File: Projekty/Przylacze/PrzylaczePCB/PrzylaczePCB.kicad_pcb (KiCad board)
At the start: 2 copper layers, 134.6 x 126 mm, 131 parts, among them J1 Conn_02x20_Odd_Even, J2 USB_B, J3 Conn_01x06, J4 Conn_02x04_Odd_Even, J5 Screw_Terminal_01x06, M3 MountingHole_3.2mm_M3, Q1 BC547, Q10 BC557, Q11 2N3904, Q12 2N7002, Q2 BC547, Q3 BC547, Q4 BC557, Q5 2N3904, Q6 BC557, Q7 BC557, Q8 BC547, Q9 BC557, SW1 SW_Push, SW2 SW_SPDT, SW3 SW_SPDT, SW4 SW_SPDT, SW5 SW_SPDT, SW6 SW_SPDT, SW7 SW_SPDT, SW8 SW_SPDT, SW9 SW_SPDT, U1 MCP2561-E-P, U2 ATSAM4S2AA-AU, U3 MCP2515-xSO, U4 TJA1055T_3_C,518, U5 MAX3485, U6 74AHC1G04, U7 LDL1117S33R, U8 DI78M05UAB, U9 74AHC1G04, Y1 20MHz

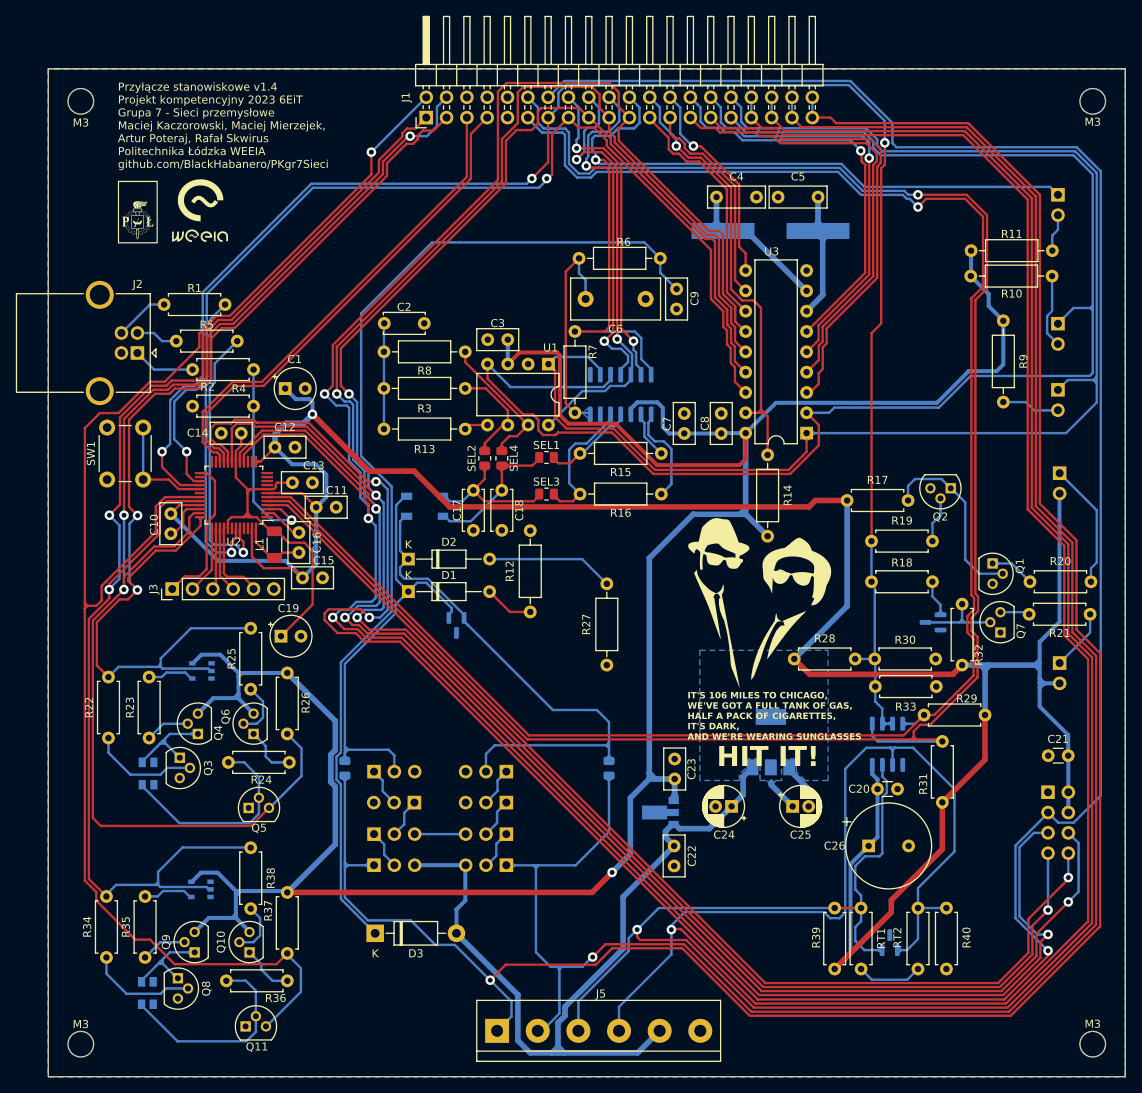
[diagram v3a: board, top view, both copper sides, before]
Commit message: Przyłącze - projekt PCB v1.5
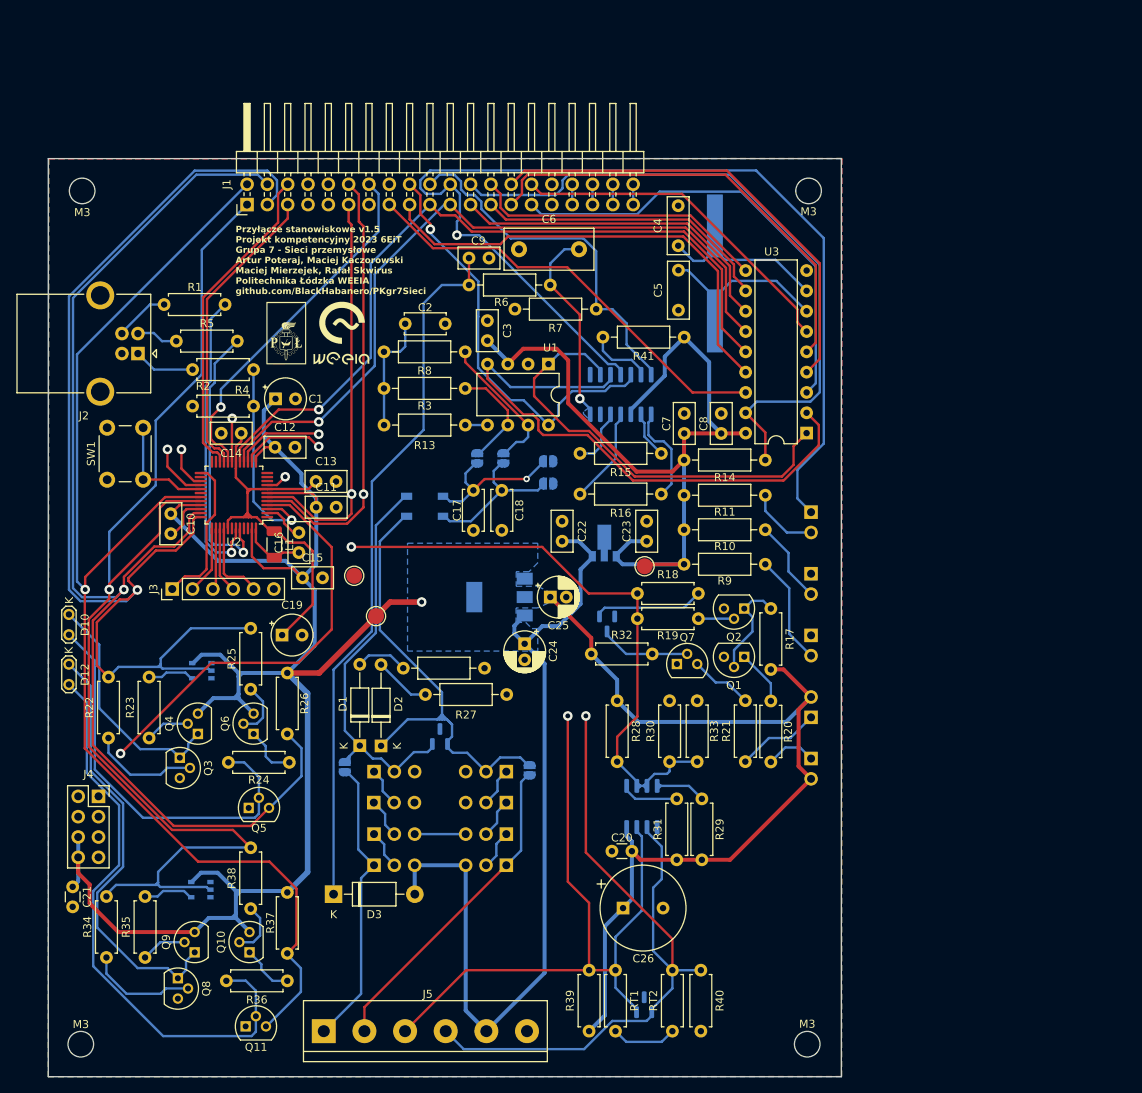
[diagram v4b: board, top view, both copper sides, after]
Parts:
- removed the G*** at (129.1, 137.9)
- added R41: 10k, Resistor_THT:R_Axial_DIN0207_L6.3mm_D2.5mm_P10.16mm_Horizontal, F.Cu at (119.6, 104.7)
- added REF**: TestPoint_Pad_D2.0mm, TestPoint:TestPoint_Pad_D2.0mm, F.Cu at (114.7, 133.3)
- added REF**: TestPoint_Pad_D2.0mm, TestPoint:TestPoint_Pad_D2.0mm, F.Cu at (81.1, 139.5)
- added REF**: TestPoint_Pad_D2.0mm, TestPoint:TestPoint_Pad_D2.0mm, F.Cu at (78.4, 134.5)
- D10, D12: footprint LED_SMD:LED_Kingbright_AAA3528ESGCT -> TestPoint:TestPoint_2Pads_Pitch2.54mm_Drill0.8mm; moved to F.Cu
- J4: moved to F.Cu
- R7: value >1k8 -> 1k
- SEL1, SEL2, SEL3, SEL4: footprint Resistor_SMD:R_0805_2012Metric -> Jumper:SolderJumper-2_P1.3mm_Open_RoundedPad1.0x1.5mm; moved to B.Cu
- SEL5, SEL6: footprint Resistor_SMD:R_0805_2012Metric -> Jumper:SolderJumper-2_P1.3mm_Open_RoundedPad1.0x1.5mm
- moved C21 123.4 mm to (43.2, 175.9), turned to 90 degrees
- moved J4 118.7 mm to (46.4, 162.1), turned to 0 degrees
- moved D4 50.3 mm to (135.5, 126.5)
- moved R10 47.9 mm to (129.8, 128.7)
- moved D7 47.3 mm to (135.5, 157.3)
- moved R11 47.1 mm to (129.8, 124.4)
- moved R21 46.9 mm to (127.3, 157.7), turned to 90 degrees
- moved R32 46.4 mm to (108.0, 144.3), turned to 0 degrees
- moved R20 45.9 mm to (130.4, 157.8), turned to 90 degrees
- moved C22 45.3 mm to (104.4, 127.7), turned to -90 degrees
- moved D6 43.9 mm to (135.5, 134.2)
- moved D5 43.5 mm to (135.5, 141.9)
- moved D12 42.3 mm to (42.7, 145.5)
- moved Q12 40.7 mm to (110.0, 140.5), turned to -90 degrees
- moved Q7 40.6 mm to (118.7, 145.5), turned to 0 degrees
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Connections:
- D9 pad 1: Net-(D1-K) -> Net-(D2-K)
- D9 pad 2: Net-(D2-K) -> Net-(D1-K)
- J1 pad 18: STB_FT -> STBY
- J1 pad 27: TX0RTS -> TX1RTS
- J1 pad 28: TX2RTS -> TX0RTS
- J1 pad 30: TX1RTS -> TX2RTS
- J1 pad 33: A -> B
- J1 pad 34: A -> B
- J1 pad 35: B -> A
- J1 pad 36: B -> A
- J1 pad 37: CANL -> CANH
- J1 pad 38: CANL -> CANH
- J1 pad 39: CANH -> CANL
- J1 pad 40: CANH -> CANL
- J1 pad 5: UART0_RX -> UART0_TX
- J1 pad 6: GND -> UART0_RX
- J1 pad 7: UART0_TX -> GND
- J4 pad 1: GND -> MISO
- J4 pad 2: +3.3V -> RADIO_IRQ
- J4 pad 3: CS0 -> SPCK
- J4 pad 4: +3.3V -> MOSI
- J4 pad 5: SPCK -> CS0
- J4 pad 6: MOSI -> +3.3V
- J4 pad 7: MISO -> GND
- J4 pad 8: RADIO_IRQ -> +3.3V
- Q10 pad 3: +5V -> +3.3V
- Q4 pad 3: +5V -> +3.3V
- Q6 pad 3: +5V -> +3.3V
- Q9 pad 3: +5V -> +3.3V
- R15 pad 2: CANH_FT -> CANL_FT
- R16 pad 1: Net-(U4-RTH) -> CANH_FT
- R16 pad 2: CANL_FT -> Net-(U4-RTH)
- R26 pad 2: +5V -> +3.3V
- R37 pad 2: +5V -> +3.3V
- R7 pad 2: Net-(U4-BAT) -> GND
- U1 pad 8: STB_FT -> STBY
- U2 pad 14: unconnected-(U2-PA16/PGMD4-Pad14) -> STBY
- U2 pad 15: unconnected-(U2-PA15/PGMD3-Pad15) -> EN
- U2 pad 9: unconnected-(U2-PA17/PGMD5/AD0-Pad9) -> ERR
- U4 pad 5: STB_FT -> STBY
- U6 pad 5: +5V -> +3.3V
- U9 pad 5: +5V -> +3.3V
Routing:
- net CS0: track 352.5 -> 120.3 mm, vias 3 -> 1
- net +5V: track 321.7 -> 104.6 mm, vias 1 -> 0
- net A: track 299.6 -> 162.0 mm
- net SPCK: track 290.4 -> 156.4 mm, vias 4 -> 1
- net RX_MCU: track 246.1 -> 118.9 mm
- net CANH: track 267.9 -> 142.4 mm, vias 1 -> 0
- net CANL: track 256.2 -> 135.4 mm, vias 1 -> 0
- net MOSI: track 281.7 -> 164.9 mm, vias 4 -> 1
- net B: track 272.7 -> 156.9 mm
- net TX_MCU: track 232.2 -> 120.1 mm
- net MISO: track 271.8 -> 162.4 mm, vias 4 -> 1
- net STBY: track 0.00 -> 92.0 mm, vias 0 -> 2
- net RADIO_IRQ: track 136.0 -> 60.9 mm
- net RXD: track 190.7 -> 117.3 mm
- net TXD: track 178.2 -> 106.9 mm
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- added copper zone on In1.Cu, net GND
- added copper zone on In2.Cu, net GND
- removed copper zone on B.Cu, net +5V
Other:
- board size 134.6 x 126 mm -> 99.1 x 114.8 mm
- copper layers 2 -> 4
- board text added: "K"
- board text added: "Przyłącze stanowiskowe v1.5 Projekt kompetencyjny 2023 6EiT Grupa 7 - Sieci przemysłowe Artur Poteraj, Maciej Kaczorowski Maciej Mierzejek, Rafał Skwirus Politechnika Łódzka WEEIA github.com/BlackHabanero/PKgr7Sieci"
- board text removed: "HIT IT!"
- board text removed: "IT'S 106 MILES TO CHICAGO, WE'VE GOT A FULL TANK OF GAS, HALF A PACK OF CIGARETTES, IT'S DARK, AND WE'RE WEARING SUNGLASSES"
- board text removed: "Przyłącze stanowiskowe v1.4 Projekt kompetencyjny 2023 6EiT Grupa 7 - Sieci przemysłowe Maciej Kaczorowski, Maciej Mierzejek, Artur Poteraj, Rafał Skwirus Politechnika Łódzka WEEIA github.com/BlackHabanero/PKgr7Sieci"

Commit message: Przyłącze - projekt PCB v1.5.1
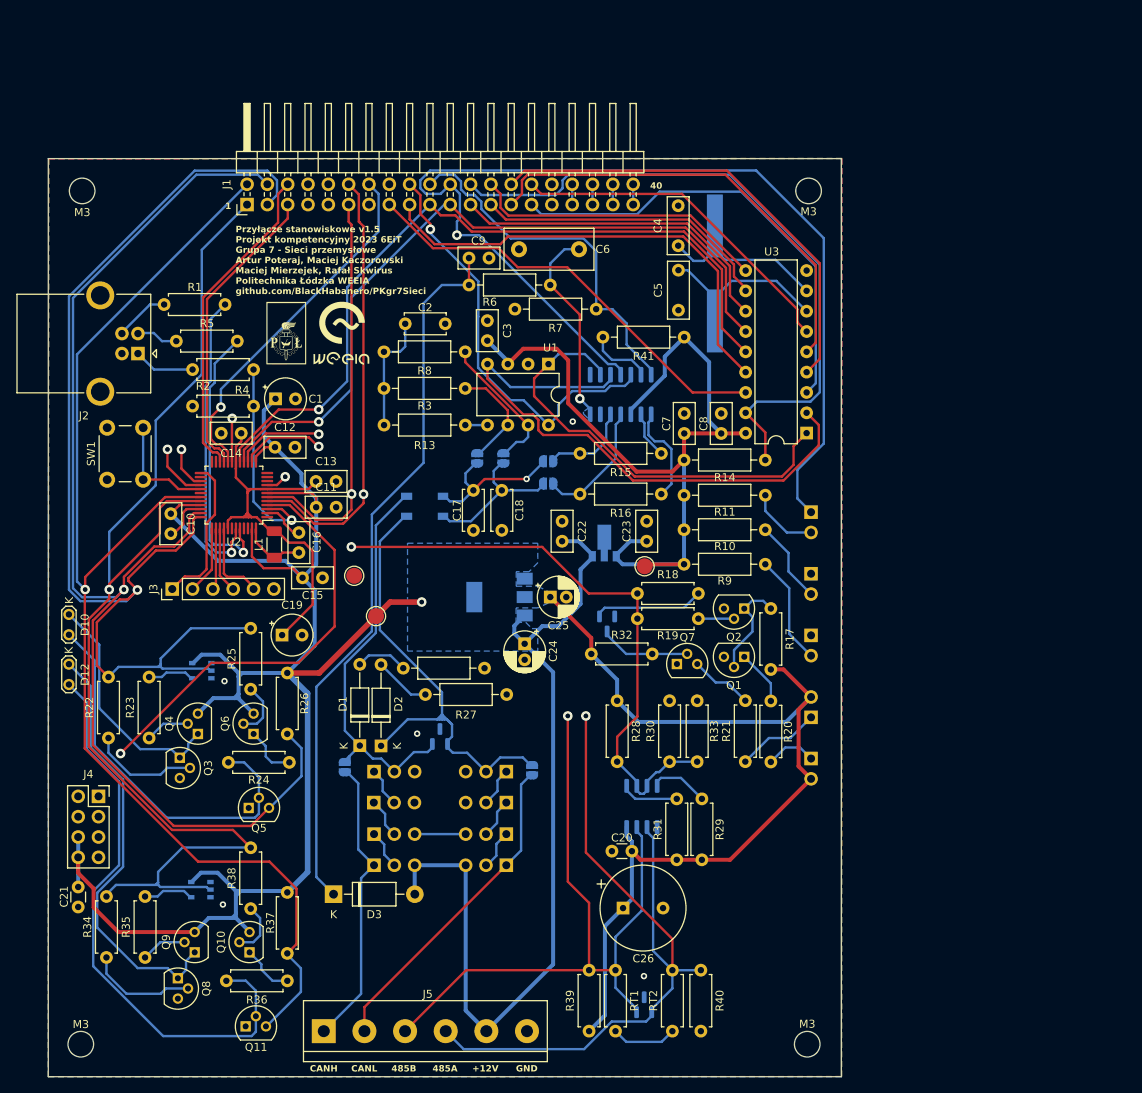
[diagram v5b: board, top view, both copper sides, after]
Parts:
- moved C21 0.69 mm to (43.9, 175.9)
- moved SEL5 0.31 mm to (100.6, 158.8)
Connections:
- R16 pad 1: CANH_FT -> Net-(U4-RTH)
- R16 pad 2: Net-(U4-RTH) -> CANH_FT
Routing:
- net CANH_FT: track 11.4 -> 15.2 mm
- net CANL_FT: track 6.80 -> 10.4 mm
- net Net-(D3-K): track 88.5 -> 90.3 mm
- net Net-(D10-A): track 50.6 -> 48.8 mm
- net RX/TX ENABLE: track 152.4 -> 151.4 mm
- net A: track 162.0 -> 161.1 mm
- net +12V: track 108.0 -> 108.9 mm
- net GND: vias 0 -> 5
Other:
- board text added: "+12V"
- board text added: "1"
- board text added: "40"
- board text added: "485A"
- board text added: "485B"
- board text added: "CANH"
- board text added: "CANL"
- board text added: "GND"
